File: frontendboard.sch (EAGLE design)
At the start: 55 parts, among them U1 MAX2769, U2 SD_CARD_SOCKET4UCON, X3 BU-SMA-H

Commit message: Signal wiring good except SDIO. Needs power fixed.
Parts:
- removed JP3: M12LOCK_LONGPADS, SparkFun-Connectors:M12LOCK_LONGPADS
- removed JTAG2: (no value), microbuilder:JTAG-CORTEXM3MOLEX
- removed U$5: USB3318, SparkFun:USB3318
- removed U2: SD_CARD_SOCKET4UCON, SparkFun-Connectors:SD_CARD_SOCKET4UCON
- added FTDI/SERIAL: (no value), microbuilder:FTDIUSBCABLE
- added HS_USB: USB3318, SparkFun:USB3318
- added SDIO: SD_CARD_SOCKET4UCON, SparkFun-Connectors:SD_CARD_SOCKET4UCON
- added SWD: (no value), microbuilder:JTAG-CORTEXM3MOLEX
- added USB_MICRO: USB_MICROB, SparkFun:USB_MICROB_PLUG-PTH
- JP1: value USB_MICROB -> M14LOCK_LONGPADS; device SparkFun:USB_MICROB_PLUG-PTH -> SparkFun-Connectors:M14LOCK_LONGPADS
- JP2: value M12LOCK_LONGPADS -> M14LOCK_LONGPADS; device SparkFun-Connectors:M12LOCK_LONGPADS -> SparkFun-Connectors:M14LOCK_LONGPADS
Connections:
- removed net CS: R5.1, U1.!CS
- removed net I2C_SCL: U$3.PB6, U1.SCLK
- removed net I2C_SDA: U$3.PB7, U1.SDATA
- removed net SPI_MISO: U$3.PA6
- removed net SPI_NSS: U$3.PA4
- removed net SPI_SCK: U$3.PB3
- new net SPI_CLK: JP1.3, JP2.3, U$3.PB3, U1.SCLK
- new net SPI_CS: JP1.2, JP2.2, R5.1, U$3.PA4, U1.!CS
- net 3.3V: now also FTDI/SERIAL.VCC, HS_USB.VDD33, HS_USB.VDDIO, SWD.1; no longer JTAG2.1, U$5.VDD33, U$5.VDDIO
- net 5.0V: now also HS_USB.VBAT; no longer U$5.VBAT
- net ANTFLAG: now also JP1.8, JP2.8, U$3.PD10
- net BAR_GND: now also BAT1.-, FTDI/SERIAL.GND, HS_USB.GND1, HS_USB.GND2, SWD.3, SWD.5, SWD.9, USB_MICRO.GND; no longer BAT1.+, JP1.GND, JTAG2.3, JTAG2.5, JTAG2.9, U$5.GND1, U$5.GND2
- net CLKOUT: now also JP1.14, JP2.14, U$3.PC6
- net CTS: now also FTDI/SERIAL.CTS
- net I0: now also JP1.11, JP2.11, U$3.PD13
- net I1: now also JP1.10, JP2.10, U$3.PD12
- net IDLE: now also JP1.9, JP2.9, U$3.PD11
- net LD: now also JP1.6, JP2.6, U$3.PD8
- net MCO1: now also HS_USB.REFCLK; no longer U$5.REFCLK
- net N$4: now also HS_USB.VDD18; no longer U$5.VDD18
- net N$5: now also HS_USB.RBIAS; no longer U$5.RBIAS
- net OTG_HS_ULPI_CLK: now also HS_USB.CLKOUT; no longer U$5.CLKOUT
- net OTG_HS_ULPI_D0: now also HS_USB.DATA0; no longer U$5.DATA0
- net OTG_HS_ULPI_D1: now also HS_USB.DATA1; no longer U$5.DATA1
- net OTG_HS_ULPI_D2: now also HS_USB.DATA2; no longer U$5.DATA2
- net OTG_HS_ULPI_D3: now also HS_USB.DATA3; no longer U$5.DATA3
- net OTG_HS_ULPI_D4: now also HS_USB.DATA4; no longer U$5.DATA4
- net OTG_HS_ULPI_D5: now also HS_USB.DATA5; no longer U$5.DATA5
- net OTG_HS_ULPI_D6: now also HS_USB.DATA6; no longer U$5.DATA6
- net OTG_HS_ULPI_D7: now also HS_USB.DATA7; no longer U$5.DATA7
- net OTG_HS_ULPI_DIR: now also HS_USB.DIR; no longer U$5.DIR
- net OTG_HS_ULPI_NXT: now also HS_USB.NXT; no longer U$5.NXT
- net OTG_HS_ULPI_STP: now also HS_USB.STP; no longer U$5.STP
- net PGM: now also JP1.7, JP2.7, U$3.PD9
- net Q0: now also JP1.12, JP2.12, U$3.PD14
- net Q1: now also JP1.13, JP2.13, U$3.PD15
- net RTS: now also FTDI/SERIAL.RTS
- net RXD: now also FTDI/SERIAL.TXD
- net SHDN: now also JP1.5, JP2.5, U$3.PB15
- net SPI_MOSI: now also JP1.4, JP2.4, U1.SDATA
- net SWCLK: now also SWD.4; no longer JTAG2.4
- net SWDIO: now also SWD.2; no longer JTAG2.2
- net TXD: now also FTDI/SERIAL.RXD
- net USB_D+: now also HS_USB.DP, USB_MICRO.D+; no longer JP1.D+, U$5.DP
- net USB_D-: now also HS_USB.DM, USB_MICRO.D-; no longer JP1.D-, U$5.DM
- net VBAT: now also BAT1.+; no longer BAT1.-
- net VBUS: now also HS_USB.VBUS, USB_MICRO.VCC; no longer JP1.VCC, U$5.VBUS
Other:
- moved on the sheet: BAT1, C1, C23, C26, C27, C28, C29, C30, Q1, R1, R10, R7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

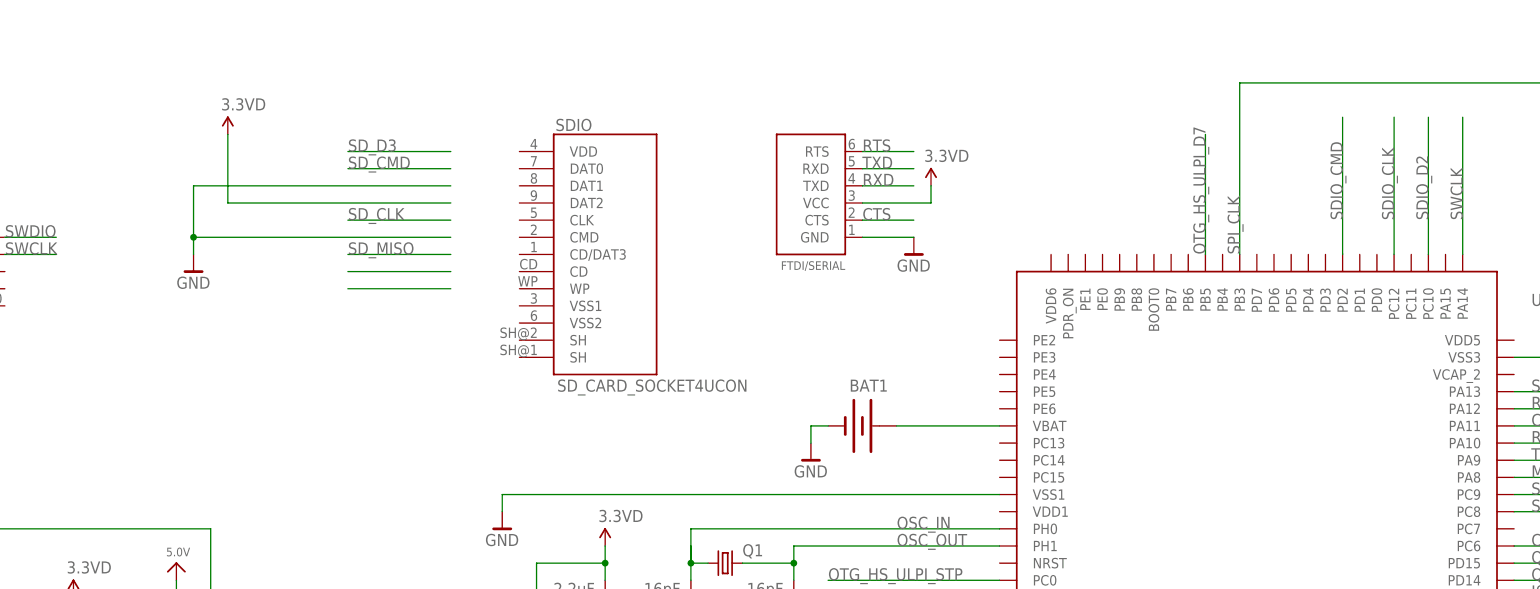
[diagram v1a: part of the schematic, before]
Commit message: SDIO wired. Still needs power fixed.
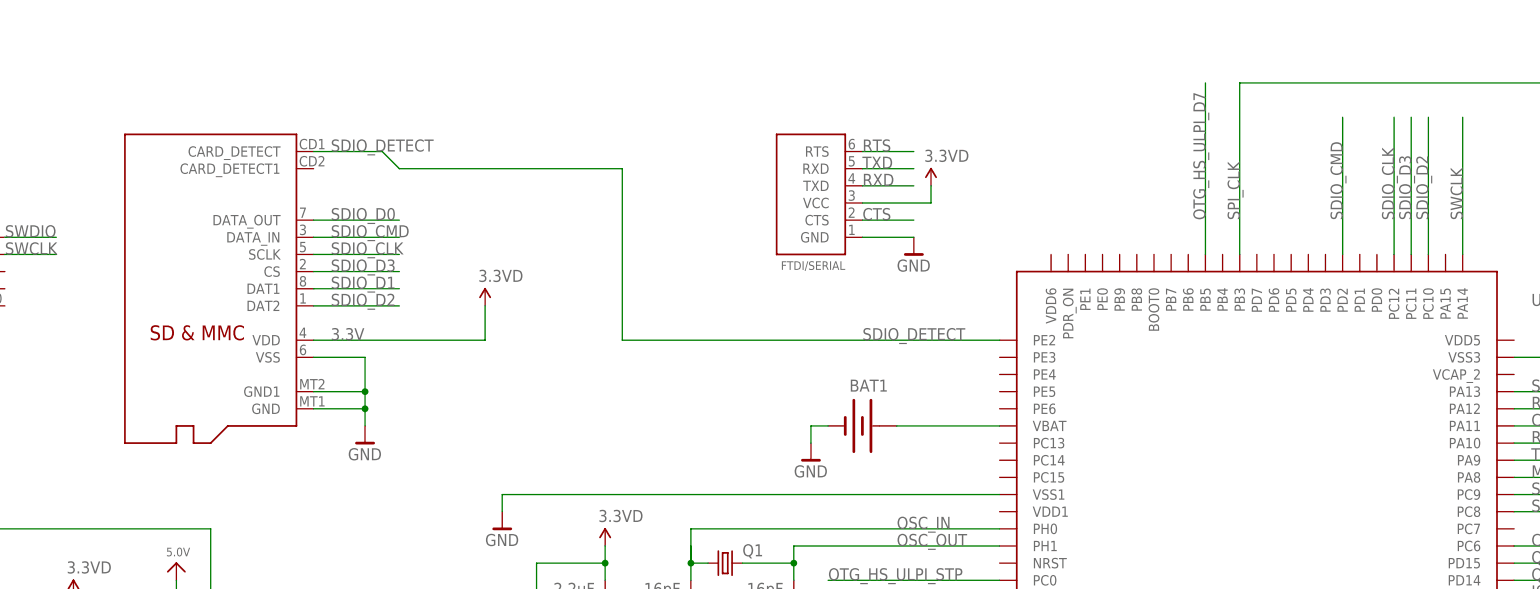
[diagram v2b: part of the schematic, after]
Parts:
- removed SDIO: SD_CARD_SOCKET4UCON, SparkFun-Connectors:SD_CARD_SOCKET4UCON
- added U$5: MICROSD, adafruit:MICROSD
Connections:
- new net SDIO_D3: U$3.PC11, U$5.CS
- new net SDIO_DETECT: U$3.PE2, U$5.CARD_DETECT
- net 3.3V: now also U$5.VDD
- net BAR_GND: now also U$5.GND, U$5.GND1, U$5.VSS
- net SDIO_CLK: now also U$5.SCLK
- net SDIO_CMD: now also U$5.DATA_IN
- net SDIO_D0: now also U$5.DATA_OUT
- net SDIO_D1: now also U$5.DAT1
- net SDIO_D2: now also U$5.DAT2

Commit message: All 3.3v is either 3.3VA or 3.3VD for analog or digital. Only power issues are on STM board.
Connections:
- removed net 3.3V: C1.2, C12.1, C13.1, C14.1, C15.1, C16.1, C17.1, C18.1, C20.1, C21.1, C28.2, C5.1, C6.1, C7.1, C8.1, C9.1, FTDI/SERIAL.VCC, HS_USB.VDD33, HS_USB.VDDIO, QG1.VCC, R1.2, R4.2, R5.2, R7.2, SWD.1, U$5.VDD, U1.VCCADC, U1.VCCCP, U1.VCCD, U1.VCCIF, U1.VCCRF, U1.VCCVCO
- net 3.3VA: now also C12.1, C13.1, C14.1, C15.1, C16.1, C18.1, C5.1, C6.1, C7.1, C8.1, R4.2, U1.VCCCP, U1.VCCD, U1.VCCIF, U1.VCCRF, U1.VCCVCO
- net 3.3VD: now also C1.2, C17.1, C20.1, C21.1, C28.2, C9.1, FTDI/SERIAL.VCC, HS_USB.VDD33, HS_USB.VDDIO, QG1.VCC, R1.2, R5.2, R7.2, SWD.1, U$5.VDD, U1.VCCADC
- net 5.0V: now also C26.2, R10.1, USB_MICRO.VCC
- net VBUS: no longer C26.2, R10.1, USB_MICRO.VCC
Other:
- moved on the sheet: C10, C11, C12, C13, C14, C15, C16, C17, C18, C19, C2, C20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

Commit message: Power wired to STM32F4. Chip looks good. How to wire BOOT?
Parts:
- added C31, C37: 2.2uF, rcl_custom:C-EU0603-B
- added C32, C34, C35, C36, C38: 100nF, rcl_custom:C-EU0603-B
- added C33: 4.7uF, rcl_custom:C-EU0603-B
- added C39: 1uF, rcl_custom:C-EU0603-B
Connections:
- new net BOOT0: U$3.BOOT0
- new net N$6: C37.2, U$3.VCAP_1
- new net VCAP_2: C31.2, U$3.VCAP_2
- net 3.3VD: now also C32.2, C33.2, C34.2, C35.2, C36.2, C38.2, C39.2, U$3.VDD1, U$3.VDD2, U$3.VDD3, U$3.VDD4, U$3.VDD5, U$3.VDD6, U$3.VDDA
- net BAR_GND: now also C31.1, C32.1, C33.1, C34.1, C35.1, C36.1, C37.1, C38.1, C39.1
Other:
- moved on the sheet: FTDI/SERIAL, U$1, U$2

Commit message: Swapped out crystal and reg for smaller packages.
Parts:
- removed QG1: TC49C, crystal:TC49C
- added Q2: (no value), crystal:CRYSTALCTS406
- U$1, U$2: value V_REG_LD1117VXX -> (none); device SparkFun:V_REG_LD1117VXX -> microbuilder:LM1117SOT223-REFLOW
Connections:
- removed net BOOT0: U$3.BOOT0
- net 3.3VD: now also Q2.1, U$3.VREF+; no longer QG1.VCC
- net BAR_GND: now also U$1.ADJ, U$2.ADJ; no longer QG1.GND, QG1.GND1, U$1.GND, U$2.GND
- net N$3: now also Q2.2; no longer QG1.OUT

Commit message: Saving it before Andrew touches it.
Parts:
- removed C20: 0.1uF, rcl_custom:C-EU0603-B
- removed C21: 0.1nF, rcl_custom:C-EU0603-B
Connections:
- net 3.3VD: no longer C20.1, C21.1, Q2.1
- net BAR_GND: now also Q2.1; no longer C20.2, C21.2
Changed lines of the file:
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@@
 <grid distance="0.1" unitdist="inch" unit="inch" style="lines" multiple="1" display="no" altdistance="0.01" altunitdist="inch" altunit="inch"/>
 <layers>
-<layer number="1" name="Top" color="4" fill="1" visible="yes" active="no"/>
-<layer number="2" name="Route2" color="1" fill="3" visible="yes" active="no"/>
-<layer number="3" name="Route3" color="4" fill="3" visible="yes" active="no"/>
-<layer number="14" name="Route14" color="1" fill="6" visible="yes" active="no"/>
-<layer number="15" name="Route15" color="4" fill="6" visible="yes" active="no"/>
-<layer number="16" name="Bottom" color="1" fill="1" visible="yes" active="no"/>
-<layer number="17" name="Pads" color="2" fill="1" visible="yes" active="no"/>
-<layer number="18" name="Vias" color="2" fill="1" visible="yes" active="no"/>
-<layer number="19" name="Unrouted" color="6" fill="1" visible="yes" active="no"/>
-<layer number="20" name="Dimension" color="15" fill="1" visible="yes" active="no"/>
-<layer number="21" name="tPlace" color="7" fill="1" visible="yes" active="no"/>
-<layer number="22" name="bPlace" color="13" fill="1" visible="yes" active="no"/>
-<layer number="23" name="tOrigins" color="15" fill="1" visible="yes" active="no"/>
-<layer number="24" name="bOrigins" color="15" fill="1" visible="yes" active="no"/>
-<layer number="25" name="tNames" color="2" fill="1" visible="yes" active="no"/>
-<layer number="26" name="bNames" color="10" fill="1" visible="yes" active="no"/>
-<layer number="27" name="tValues" color="7" fill="1" visible="yes" active="no"/>
-<layer number="28" name="bValues" color="7" fill="1" visible="yes" active="no"/>
+<layer number="1" name="Top" color="4" fill="1" visible="no" active="no"/>
+<layer number="2" name="Route2" color="1" fill="3" visible="no" active="no"/>
+<layer number="3" name="Route3" color="4" fill="3" visible="no" active="no"/>
+<layer number="14" name="Route14" color="1" fill="6" visible="no" active="no"/>
+<layer number="15" name="Route15" color="4" fill="6" visible="no" active="no"/>
+<layer number="16" name="Bottom" color="1" fill="1" visible="no" active="no"/>
+<layer number="17" name="Pads" color="2" fill="1" visible="no" active="no"/>
+<layer number="18" name="Vias" color="2" fill="1" visible="no" active="no"/>
+<layer number="19" name="Unrouted" color="6" fill="1" visible="no" active="no"/>
+<layer number="20" name="Dimension" color="15" fill="1" visible="no" active="no"/>
+<layer number="21" name="tPlace" color="7" fill="1" visible="no" active="no"/>
+<layer number="22" name="bPlace" color="13" fill="1" visible="no" active="no"/>
+<layer number="23" name="tOrigins" color="15" fill="1" visible="no" active="no"/>
+<layer number="24" name="bOrigins" color="15" fill="1" visible="no" active="no"/>
+<layer number="25" name="tNames" color="2" fill="1" visible="no" active="no"/>
+<layer number="26" name="bNames" color="10" fill="1" visible="no" active="no"/>
+<layer number="27" name="tValues" color="7" fill="1" visible="no" active="no"/>
+<layer number="28" name="bValues" color="7" fill="1" visible="no" active="no"/>
 <layer number="29" name="tStop" color="7" fill="3" visible="no" active="no"/>
 <layer number="30" name="bStop" color="7" fill="6" visible="no" active="no"/>
@@
 <layer number="35" name="tGlue" color="7" fill="4" visible="no" active="no"/>
 <layer number="36" name="bGlue" color="7" fill="5" visible="no" active="no"/>
-<layer number="37" name="tTest" color="7" fill="1" visible="yes" active="no"/>
-<layer number="38" name="bTest" color="7" fill="1" visible="yes" active="no"/>
+<layer number="37" name="tTest" color="7" fill="1" visible="no" active="no"/>
+<layer number="38" name="bTest" color="7" fill="1" visible="no" active="no"/>
 <layer number="39" name="tKeepout" color="4" fill="11" visible="no" active="no"/>
 <layer number="40" name="bKeepout" color="1" fill="11" visible="no" active="no"/>
@@
 <layer number="44" name="Drills" color="7" fill="1" visible="no" active="no"/>
 <layer number="45" name="Holes" color="7" fill="1" visible="no" active="no"/>
-<layer number="46" name="Milling" color="3" fill="1" visible="yes" active="no"/>
-<layer number="47" name="Measures" color="7" fill="1" visible="yes" active="no"/>
-<layer number="48" name="Document" color="7" fill="1" visible="yes" active="no"/>
-<layer number="49" name="Reference" color="7" fill="1" visible="yes" active="no"/>
-<layer number="50" name="dxf" color="7" fill="1" visible="yes" active="no"/>
-<layer number="51" name="tDocu" color="14" fill="1" visible="yes" active="no"/>
-<layer number="52" name="bDocu" color="7" fill="1" visible="yes" active="no"/>
-<layer number="53" name="tGND_GNDA" color="7" fill="9" visible="yes" active="no"/>
-<layer number="54" name="bGND_GNDA" color="1" fill="9" visible="yes" active="no"/>
-<layer number="56" name="wert" color="7" fill="1" visible="yes" active="no"/>
+<layer number="46" name="Milling" color="3" fill="1" visible="no" active="no"/>
+<layer number="47" name="Measures" color="7" fill="1" visible="no" active="no"/>
+<layer number="48" name="Document" color="7" fill="1" visible="no" active="no"/>
+<layer number="49" name="Reference" color="7" fill="1" visible="no" active="no"/>
+<layer number="50" name="dxf" color="7" fill="1" visible="no" active="no"/>
+<layer number="51" name="tDocu" color="14" fill="1" visible="no" active="no"/>
+<layer number="52" name="bDocu" color="7" fill="1" visible="no" active="no"/>
+<layer number="53" name="tGND_GNDA" color="7" fill="9" visible="no" active="no"/>
+<layer number="54" name="bGND_GNDA" color="1" fill="9" visible="no" active="no"/>
+<layer number="56" name="wert" color="7" fill="1" visible="no" active="no"/>
 <layer number="91" name="Nets" color="2" fill="1" visible="yes" active="yes"/>
 <layer number="92" name="Busses" color="1" fill="1" visible="yes" active="yes"/>
@@
 <part name="DIG_GND18" library="supply" deviceset="GND_BAR" device="" value="GND"/>
 <part name="DIG_GND19" library="supply" deviceset="GND_BAR" device="" value="GND"/>
-<part name="C20" library="rcl_custom" deviceset="C-EU" device="0603-B" value="0.1uF"/>
-<part name="C21" library="rcl_custom" deviceset="C-EU" device="0603-B" value="0.1nF"/>
-<part name="DIG_GND7" library="supply" deviceset="GND_BAR" device="" value="GND"/>
-<part name="DIG_GND22" library="supply" deviceset="GND_BAR" device="" value="GND"/>
 <part name="R4" library="rcl_custom" deviceset="R-US_" device="0603-B" value="20k"/>
 <part name="R5" library="rcl_custom" deviceset="R-US_" device="0603-B" value="20k"/>
@@
 <part name="R7" library="rcl_custom" deviceset="R-US_" device="0603-B" value="1.5k"/>
 <part name="3.3VD" library="SparkFun" deviceset="3.3V" device="" value="3.3VD"/>
-<part name="3.3VD1" library="SparkFun" deviceset="3.3V" device="" value="3.3VD"/>
 <part name="3.3VD2" library="SparkFun" deviceset="3.3V" device="" value="3.3VD"/>
 <part name="3.3VA" library="SparkFun" deviceset="3.3V" device="" value="3.3VA"/>
@@
 <part name="DIG_GND53" library="supply" deviceset="GND_BAR" device="" value="GND"/>
 <part name="Q2" library="crystal" deviceset="CRYSTAL" device="CTS406"/>
+<part name="DIG_GND7" library="supply" deviceset="GND_BAR" device="" value="GND"/>
 </parts>
 <sheets>
@@
 <instance part="DIG_GND18" gate="1" x="27.94" y="119.38"/>
 <instance part="DIG_GND19" gate="1" x="27.94" y="144.78"/>
-<instance part="C20" gate="CE" x="675.64" y="160.02"/>
-<instance part="C21" gate="CE" x="662.94" y="160.02"/>
-<instance part="DIG_GND7" gate="1" x="662.94" y="152.4"/>
-<instance part="DIG_GND22" gate="1" x="675.64" y="152.4"/>
 <instance part="R4" gate="R" x="513.08" y="88.9" rot="R90"/>
 <instance part="R5" gate="R" x="693.42" y="71.12" rot="R90"/>
@@
 <instance part="R7" gate="R" x="45.72" y="81.28" rot="MR90"/>
 <instance part="3.3VD" gate="G$1" x="45.72" y="99.06" rot="MR0"/>
-<instance part="3.3VD1" gate="G$1" x="675.64" y="167.64"/>
 <instance part="3.3VD2" gate="G$1" x="619.76" y="162.56" rot="MR0"/>
 <instance part="3.3VA" gate="G$1" x="670.56" y="134.62"/>
@@
 <instance part="DIG_GND53" gate="1" x="215.9" y="66.04"/>
 <instance part="Q2" gate="G$1" x="685.8" y="165.1"/>
+<instance part="DIG_GND7" gate="1" x="675.64" y="162.56"/>
 </instances>
 <busses>
@@
 </segment>
 <segment>
-<pinref part="C21" gate="CE" pin="2"/>
-<pinref part="DIG_GND7" gate="1" pin="BAR_GND"/>
-</segment>
-<segment>
-<pinref part="C20" gate="CE" pin="2"/>
-<pinref part="DIG_GND22" gate="1" pin="BAR_GND"/>
-</segment>
-<segment>
 <pinref part="R3" gate="R" pin="1"/>
 <pinref part="DIG_GND23" gate="1" pin="BAR_GND"/>
@@
 <pinref part="C39" gate="CE" pin="1"/>
 <wire x1="215.9" y1="68.58" x2="215.9" y2="71.12" width="0.1524" layer="91"/>
+</segment>
+<segment>
+<wire x1="683.26" y1="165.1" x2="675.64" y2="165.1" width="0.1524" layer="91"/>
+<pinref part="Q2" gate="G$1" pin="1"/>
+<pinref part="DIG_GND7" gate="1" pin="BAR_GND"/>
 </segment>
 </net>
@@
 </segment>
 <segment>
-<pinref part="3.3VD1" gate="G$1" pin="3.3V"/>
-<wire x1="675.64" y1="162.56" x2="675.64" y2="165.1" width="0.1524" layer="91"/>
-<pinref part="C20" gate="CE" pin="1"/>
-<wire x1="675.64" y1="165.1" x2="675.64" y2="167.64" width="0.1524" layer="91"/>
-<pinref part="C21" gate="CE" pin="1"/>
-<wire x1="683.26" y1="165.1" x2="675.64" y2="165.1" width="0.1524" layer="91"/>
-<wire x1="675.64" y1="165.1" x2="662.94" y2="165.1" width="0.1524" layer="91"/>
-<wire x1="662.94" y1="165.1" x2="662.94" y2="162.56" width="0.1524" layer="91"/>
-<junction x="675.64" y="165.1"/>
-<pinref part="Q2" gate="G$1" pin="1"/>
-</segment>
-<segment>

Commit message: Add buses. Complete SDIO detect circuit. Add bypass caps where needed.
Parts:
- added C20: 2.2uF, rcl_custom:C-EU0603-B
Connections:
- net 3.3VD: now also C20.2
- net BAR_GND: now also C20.1, U$5.CARD_DETECT1
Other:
- moved on the sheet: BAT1, C1, C10, C11, C12, C13, C14, C15, C16, C17, C18, C19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

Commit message: All power pins replaced with customs so no ERC fails. Still needs BOOT0/PDR_ON on STM figured out.
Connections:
- net BAR_GND: now also U1.BODY
